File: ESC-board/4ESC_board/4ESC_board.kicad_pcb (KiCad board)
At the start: 2 copper layers, 82.4 x 96.9 mm, 10 parts, among them U1 ESCPINS, U2 ESCPINS, U3 ESCPINS, U4 ESCPINS

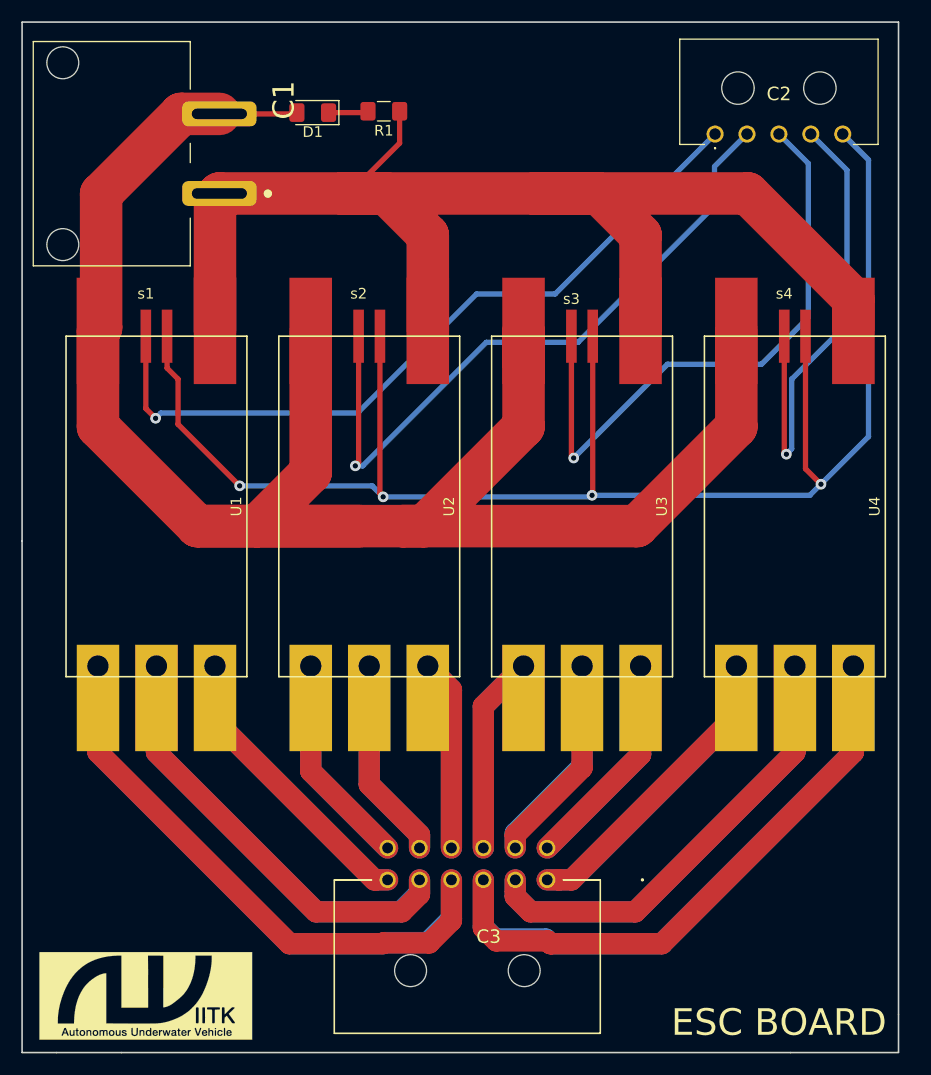
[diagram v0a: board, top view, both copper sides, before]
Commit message: power-trace plane changed, gerber-BOM generated
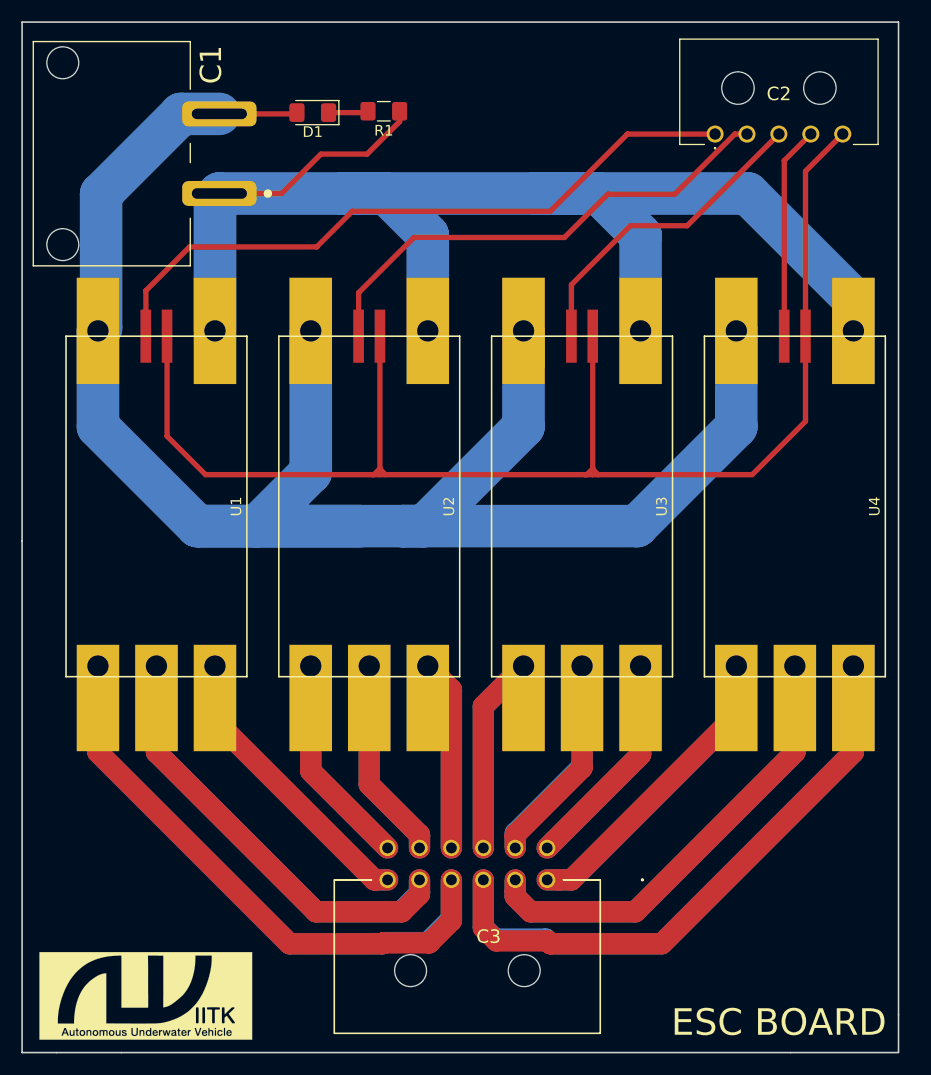
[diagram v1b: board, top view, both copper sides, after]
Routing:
- net /SPEED3: track 57.4 -> 30.2 mm, vias 1 -> 0
- net /SPEED4: track 45.0 -> 20.0 mm, vias 1 -> 0
- net /MGND: track 152.9 -> 130.9 mm, vias 4 -> 0
- net /SPEED2: track 64.2 -> 46.8 mm, vias 1 -> 0
- net /SPEED1: track 71.7 -> 63.9 mm, vias 1 -> 0
- net /GND: track 132.4 -> 139.7 mm

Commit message: added fuse
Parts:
- added F1: Fuse, minibladefuse:MCCQ-122, F.Cu at (114.1, 45.8)
- moved R1 6.23 mm to (107.3, 36.2)
- moved D1 6.04 mm to (101.5, 36.2)
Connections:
- C1 pad 2: /GND -> Net-(C1-Pad2)
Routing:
- net Net-(C1-Pad2): track 0.00 -> 18.2 mm
- net /GND: track 139.7 -> 131.3 mm
- net Net-(D1-Pad1): track 3.76 -> 2.86 mm
- net /VIN: track 183.3 -> 184.2 mm
- added copper zone on B.Cu, net Net-(C1-Pad2)
